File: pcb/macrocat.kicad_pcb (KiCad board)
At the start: 2 copper layers, 78.7 x 97.3 mm, 52 parts, among them J1 USB-C USB 2.0 MC-372, SW1 SW_Push, SW2 RotaryEncoder_Switch, U1 ATmega32U4-A, Y1 Crystal_GND24_Small

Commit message: routed by freerouter
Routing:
- net GND: track 0.00 -> 168.8 mm
- net ROW4: track 0.00 -> 136.6 mm
- net COL1: track 0.00 -> 119.6 mm, vias 0 -> 1
- net ROW3: track 0.00 -> 119.0 mm
- net COL2: track 0.00 -> 102.0 mm, vias 0 -> 1
- net +5V: track 0.00 -> 92.3 mm
- net ROW2: track 0.00 -> 90.7 mm
- net COL3: track 0.00 -> 84.2 mm, vias 0 -> 1
- net ROW1: track 0.00 -> 82.6 mm
- net COL4: track 0.00 -> 67.0 mm, vias 0 -> 1
- net KNOB1: track 0.00 -> 53.7 mm, vias 0 -> 1
- net KNOB2: track 0.00 -> 53.5 mm
- net Net-(R3-Pad2): track 0.00 -> 34.8 mm, vias 0 -> 2
- net Net-(R1-Pad2): track 0.00 -> 34.6 mm, vias 0 -> 2
- net VCC: track 0.00 -> 30.8 mm
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
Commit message: fix some bug in pcb
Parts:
- Y1: value Crystal_GND24_Small -> 16M
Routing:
- net GND: track 168.8 -> 157.3 mm
- net ROW4: track 136.6 -> 142.2 mm
- net ROW3: track 119.0 -> 124.6 mm
- net ROW1: track 82.6 -> 87.0 mm
- net D+: track 4.09 -> 7.65 mm, vias 0 -> 2
- net D-: track 6.00 -> 8.65 mm
- net Net-(R3-Pad2): track 34.8 -> 35.5 mm
- added copper zone on B.Cu, net GND
- added copper zone on F.Cu, net GND

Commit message: adjust some figures on pcb
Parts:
- J1: value USB-C USB 2.0 MC-372 -> USB-C Connector
- renumbered SW2 to KNOB1, SW1 to RESET1

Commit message: optimize mcu part wiring
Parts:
- D1, D10, D11, D12, D13, D14, D15, D16, D2, D3, D4, D5, D6, D7, D8, D9: footprint Diode_SMD:D_SOD-123 -> macrocat:D_SOD-123_back
- moved F1 2.06 mm to (115.4, 73.8)
- moved R3 2.06 mm to (110.7, 73.9)
- moved R1 1.71 mm to (127.2, 71.4)
- moved R2 1.71 mm to (124.8, 71.4)
- moved R5 1.71 mm to (127.2, 75.4)
- moved R6 1.71 mm to (124.8, 75.4)
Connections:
- U1 pad 12: unconnected-(U1-Pad12) -> KNOB_SW
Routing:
- net GND: track 157.3 -> 28.8 mm, vias 0 -> 4
- net KNOB_SW: track 0.00 -> 37.9 mm, vias 0 -> 1
- net COL3: track 84.2 -> 113.3 mm, vias 1 -> 2
- net ROW1: track 87.0 -> 71.8 mm, vias 0 -> 1
- net COL2: track 102.0 -> 115.7 mm
- net ROW4: track 142.2 -> 128.5 mm, vias 0 -> 1
- net VCC: track 30.8 -> 17.9 mm, vias 0 -> 2
- net ROW3: track 124.6 -> 112.1 mm, vias 0 -> 2
- net COL4: track 67.0 -> 77.4 mm, vias 1 -> 2
- net ROW2: track 90.7 -> 100.3 mm, vias 0 -> 1
- net Net-(R3-Pad2): track 35.5 -> 44.6 mm
- net Net-(R1-Pad2): track 34.6 -> 26.9 mm
- net Net-(R2-Pad2): track 29.1 -> 35.6 mm, vias 2 -> 0
- net +5V: track 92.3 -> 87.6 mm
- net D-: track 8.65 -> 13.0 mm
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
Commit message: add some cat
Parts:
- added G***: LOGO, LOGO, F.Cu at (111.8, 63.5)
- added G***: LOGO, LOGO, F.Cu at (154.7, 60.2)
- added G***: LOGO, LOGO, F.Cu at (158.4, 61.2)
- moved RESET1 6.80 mm to (110.7, 70.2)
- moved R3 2.25 mm to (110.7, 76.2)
- moved F1 1.78 mm to (115.4, 75.6)
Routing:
- net COL3: track 113.3 -> 82.7 mm, vias 2 -> 1
- net COL2: track 115.7 -> 100.8 mm
- net COL4: track 77.4 -> 67.8 mm, vias 2 -> 1
- net Net-(R3-Pad2): track 44.6 -> 39.0 mm
- net ROW2: track 100.3 -> 95.5 mm, vias 1 -> 5
- net ROW4: track 128.5 -> 133.2 mm, vias 1 -> 5
- net ROW1: track 71.8 -> 76.0 mm, vias 1 -> 4
- net ROW3: track 112.1 -> 114.9 mm, vias 2 -> 5
- net VCC: track 17.9 -> 19.1 mm
- net COL1: track 120.0 -> 118.9 mm
- net +5V: track 87.6 -> 86.8 mm

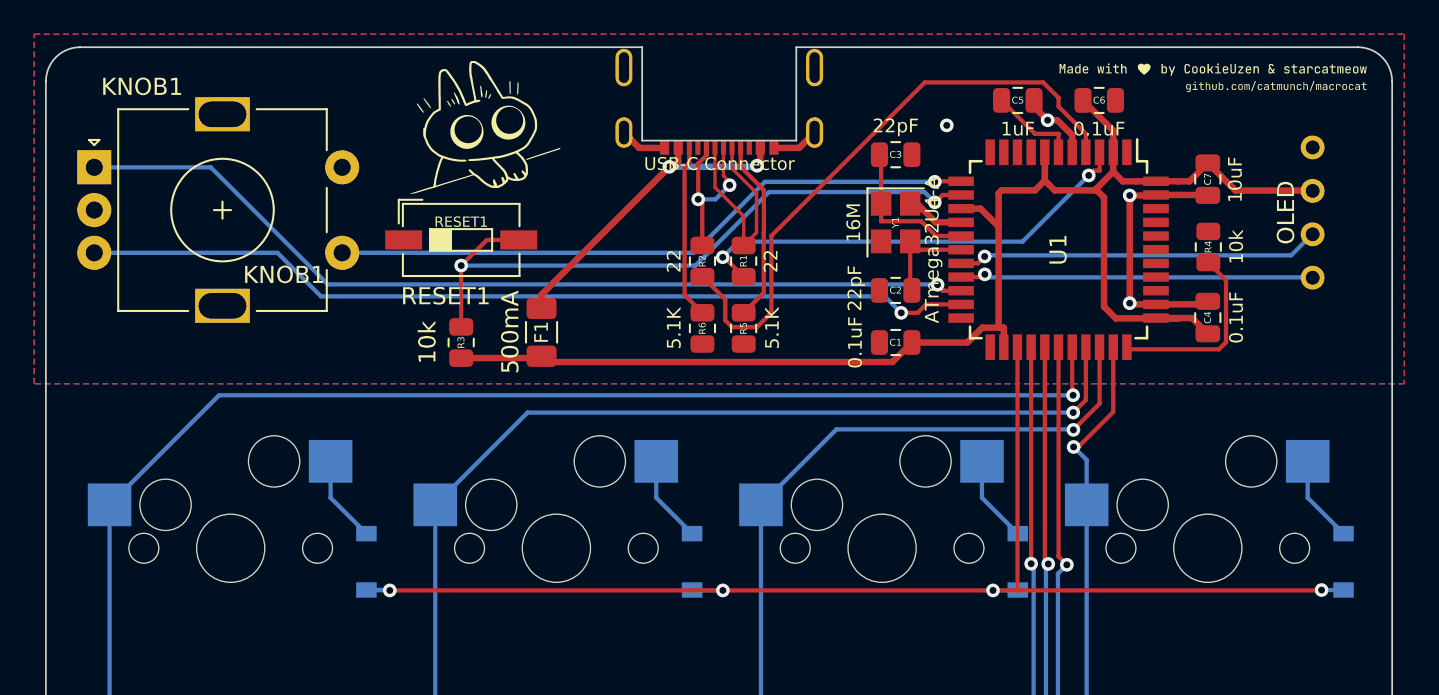
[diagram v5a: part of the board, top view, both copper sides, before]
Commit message: change mcu to atmega32u4-mu
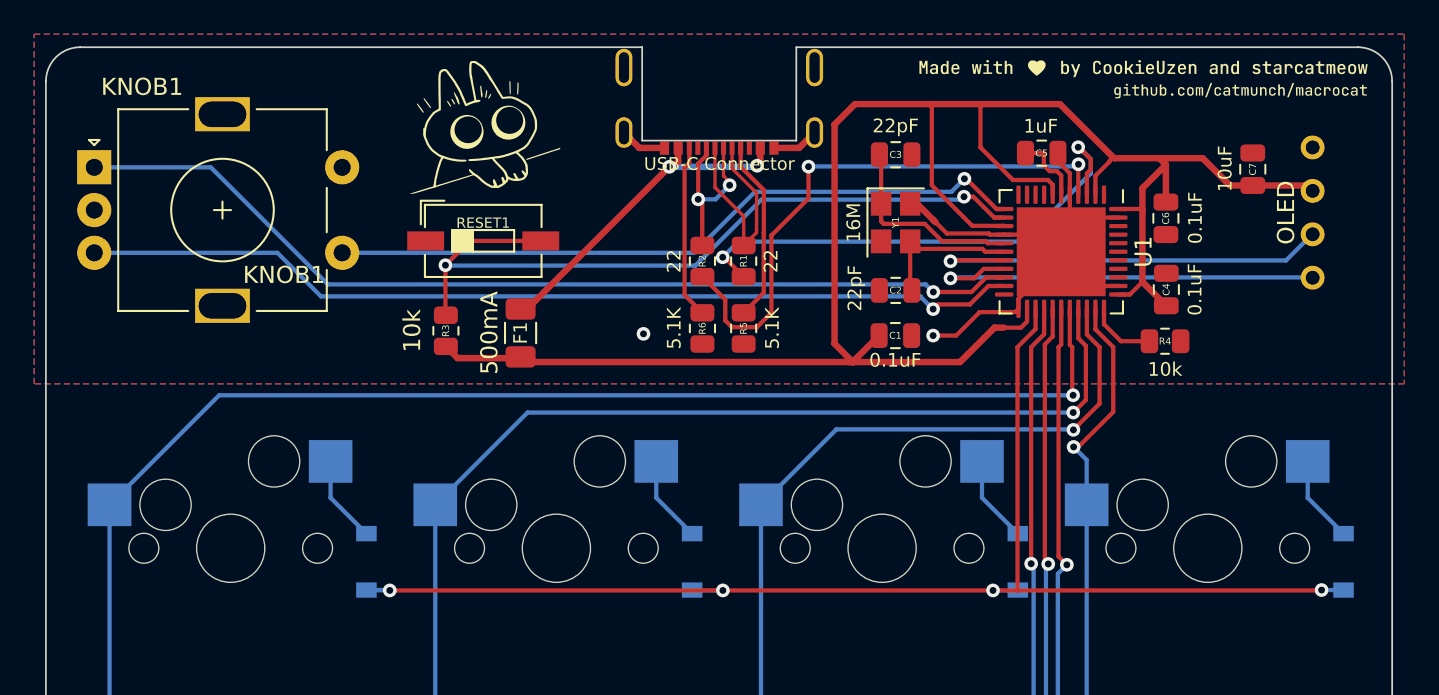
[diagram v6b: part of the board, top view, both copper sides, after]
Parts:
- removed the G*** at (154.7, 60.2)
- removed the G*** at (158.4, 61.2)
- added G***: LOGO, LOGO, F.Cu at (156.3, 61.4)
- added G***: LOGO, LOGO, F.Cu at (150.6, 60.2)
- U1: value ATmega32U4-A -> ATmega32U4-M; footprint Package_QFP:TQFP-44_10x10mm_P0.8mm -> Package_DFN_QFN:QFN-44-1EP_7x7mm_P0.5mm_EP5.2x5.2mm
- moved C6 7.92 mm to (151.9, 68.9), turned to -90 degrees
- moved R4 6.07 mm to (151.9, 76.1), turned to 0 degrees
- moved C5 3.39 mm to (144.7, 65.1)
- moved C4 2.93 mm to (151.9, 73.1)
- moved C7 2.69 mm to (157.0, 66.1), turned to 90 degrees
- moved RESET1 1.29 mm to (112.0, 70.3)
- moved F1 1.23 mm to (114.2, 75.6)
- moved R3 1.13 mm to (109.8, 75.5)
- moved C1 0.41 mm to (136.1, 75.8), turned to 0 degrees
- moved U1 0.20 mm to (145.8, 70.9)
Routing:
- net +5V: track 86.8 -> 122.6 mm
- net GND: track 28.8 -> 40.3 mm, vias 4 -> 2
- net Net-(R4-Pad1): track 11.1 -> 3.97 mm
- net Net-(R3-Pad2): track 39.0 -> 44.0 mm
- net SDA: track 20.7 -> 24.6 mm
- net SCL: track 21.3 -> 25.0 mm
- net Net-(R1-Pad2): track 26.9 -> 30.3 mm
- net KNOB_SW: track 37.9 -> 41.2 mm
- net KNOB1: track 53.7 -> 56.6 mm
- net KNOB2: track 52.4 -> 55.2 mm
- net Net-(C3-Pad2): track 8.97 -> 11.7 mm
- net ROW1: track 76.0 -> 78.7 mm
- net COL4: track 67.8 -> 70.5 mm
- net Net-(C2-Pad2): track 6.09 -> 8.66 mm
- net ROW2: track 95.5 -> 98.0 mm
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
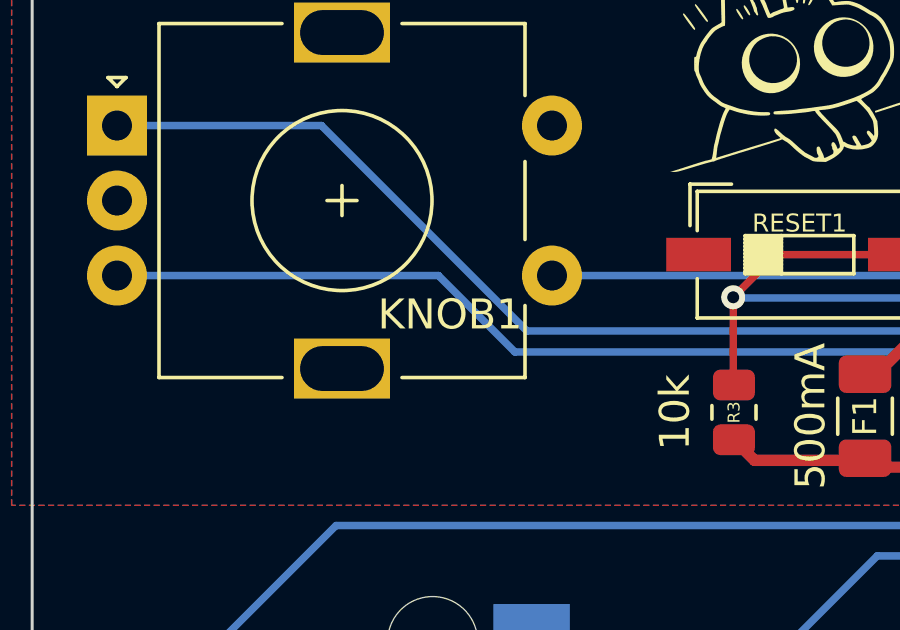
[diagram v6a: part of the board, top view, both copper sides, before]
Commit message: create 3d model
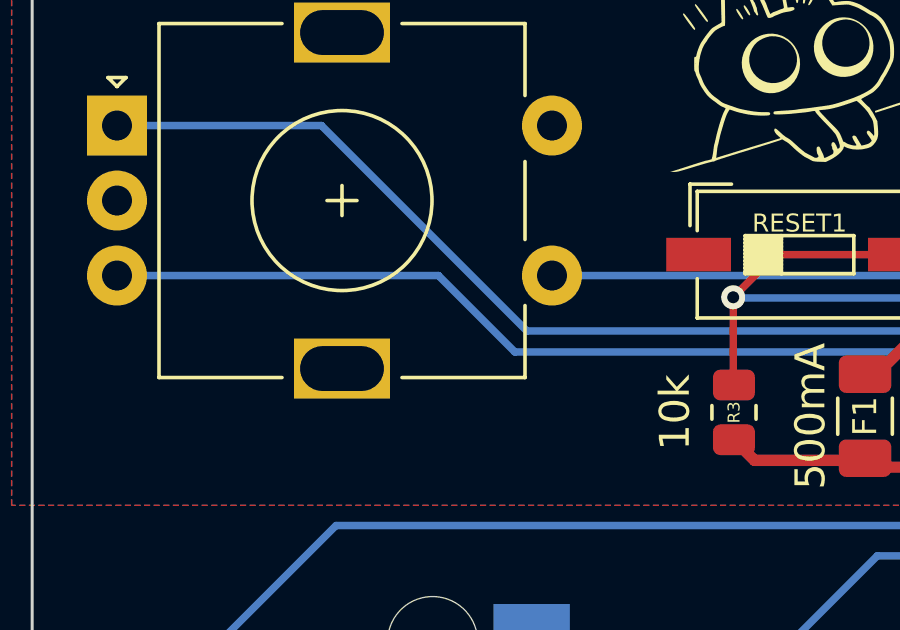
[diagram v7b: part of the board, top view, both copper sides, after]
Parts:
- KNOB1: footprint Rotary_Encoder:RotaryEncoder_Alps_EC11E-Switch_Vertical_H20mm -> macrocat:RotaryEncoder_Alps_EC11E-Switch_Vertical_H20mm
- MX1, MX10, MX11, MX12, MX13, MX14, MX15, MX16, MX2, MX3, MX4, MX5, MX6, MX7, MX8, MX9: footprint MX_Only:MXOnly-1U-Hotswap -> macrocat:MXOnly-1U-Hotswap
